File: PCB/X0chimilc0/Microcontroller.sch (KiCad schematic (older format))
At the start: 4 parts, among them T1 SDS-50J, T2 SDS-50J, T3 SDS-50J, U1 STM32H745XIH6

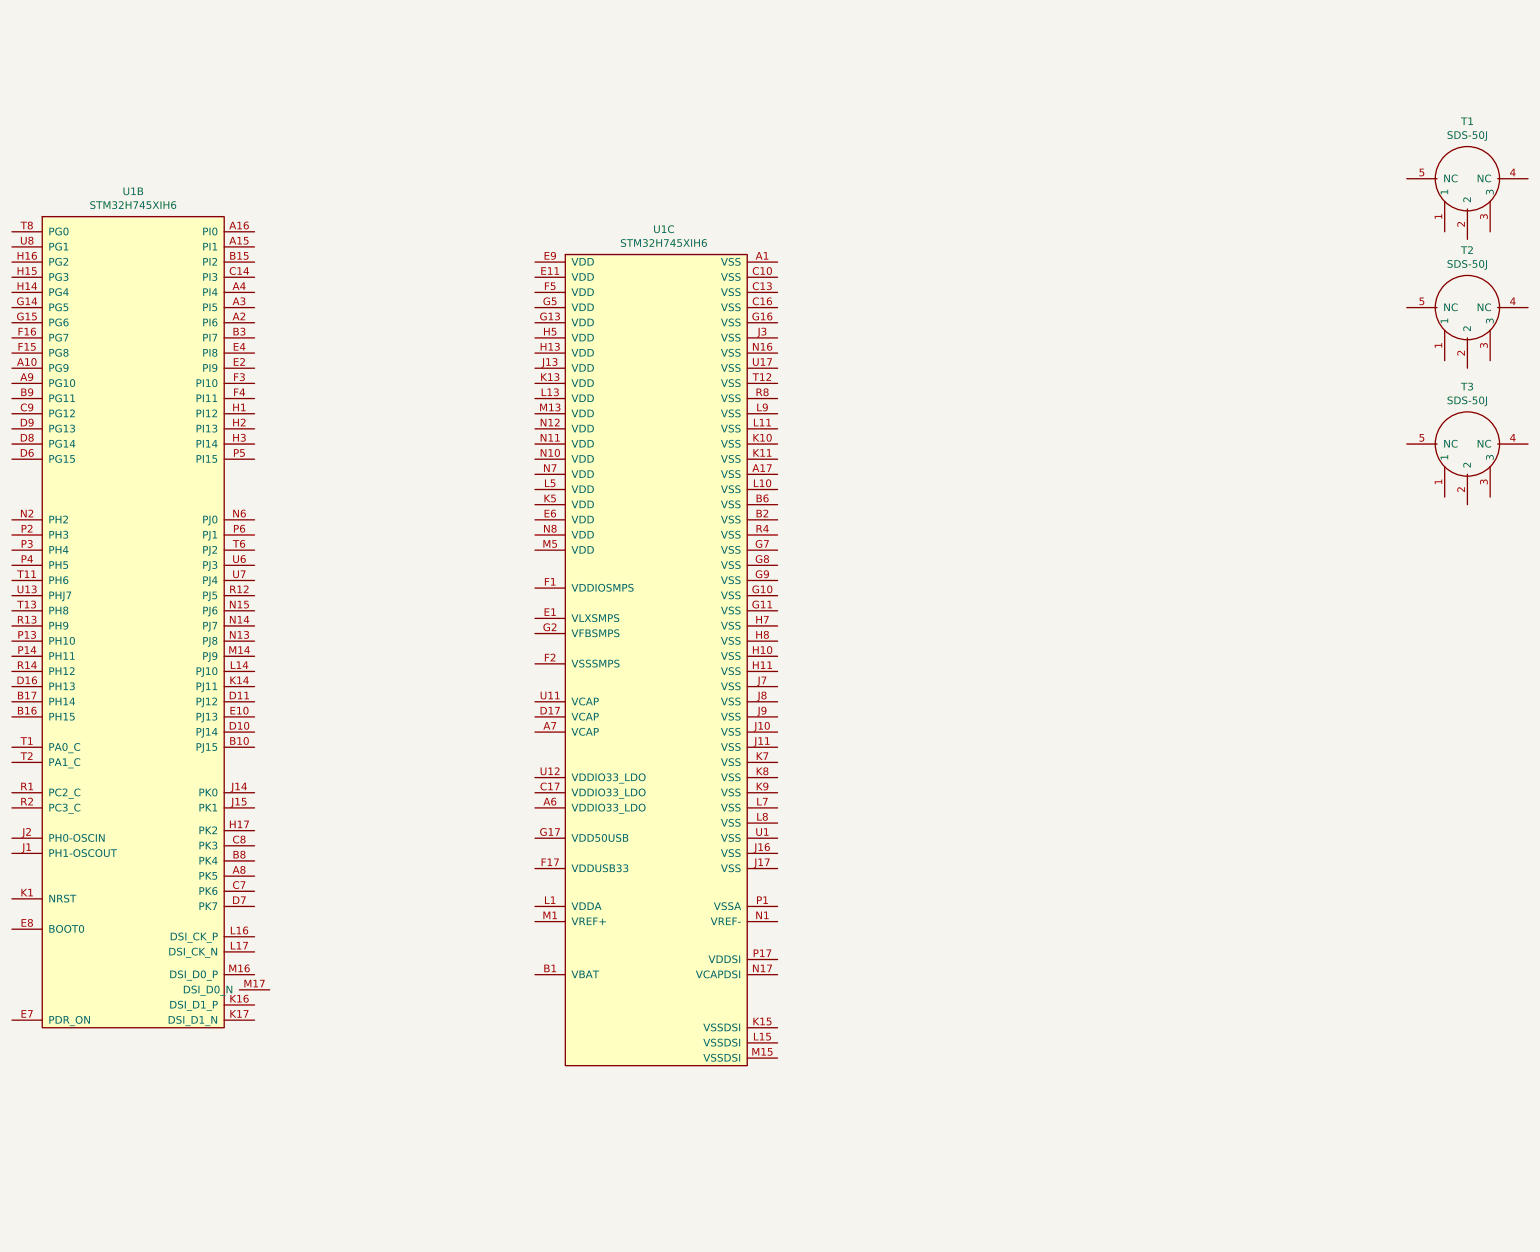
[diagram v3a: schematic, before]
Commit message: MCU Power
MCU power schematic completed, working on other MCU part and Codec.
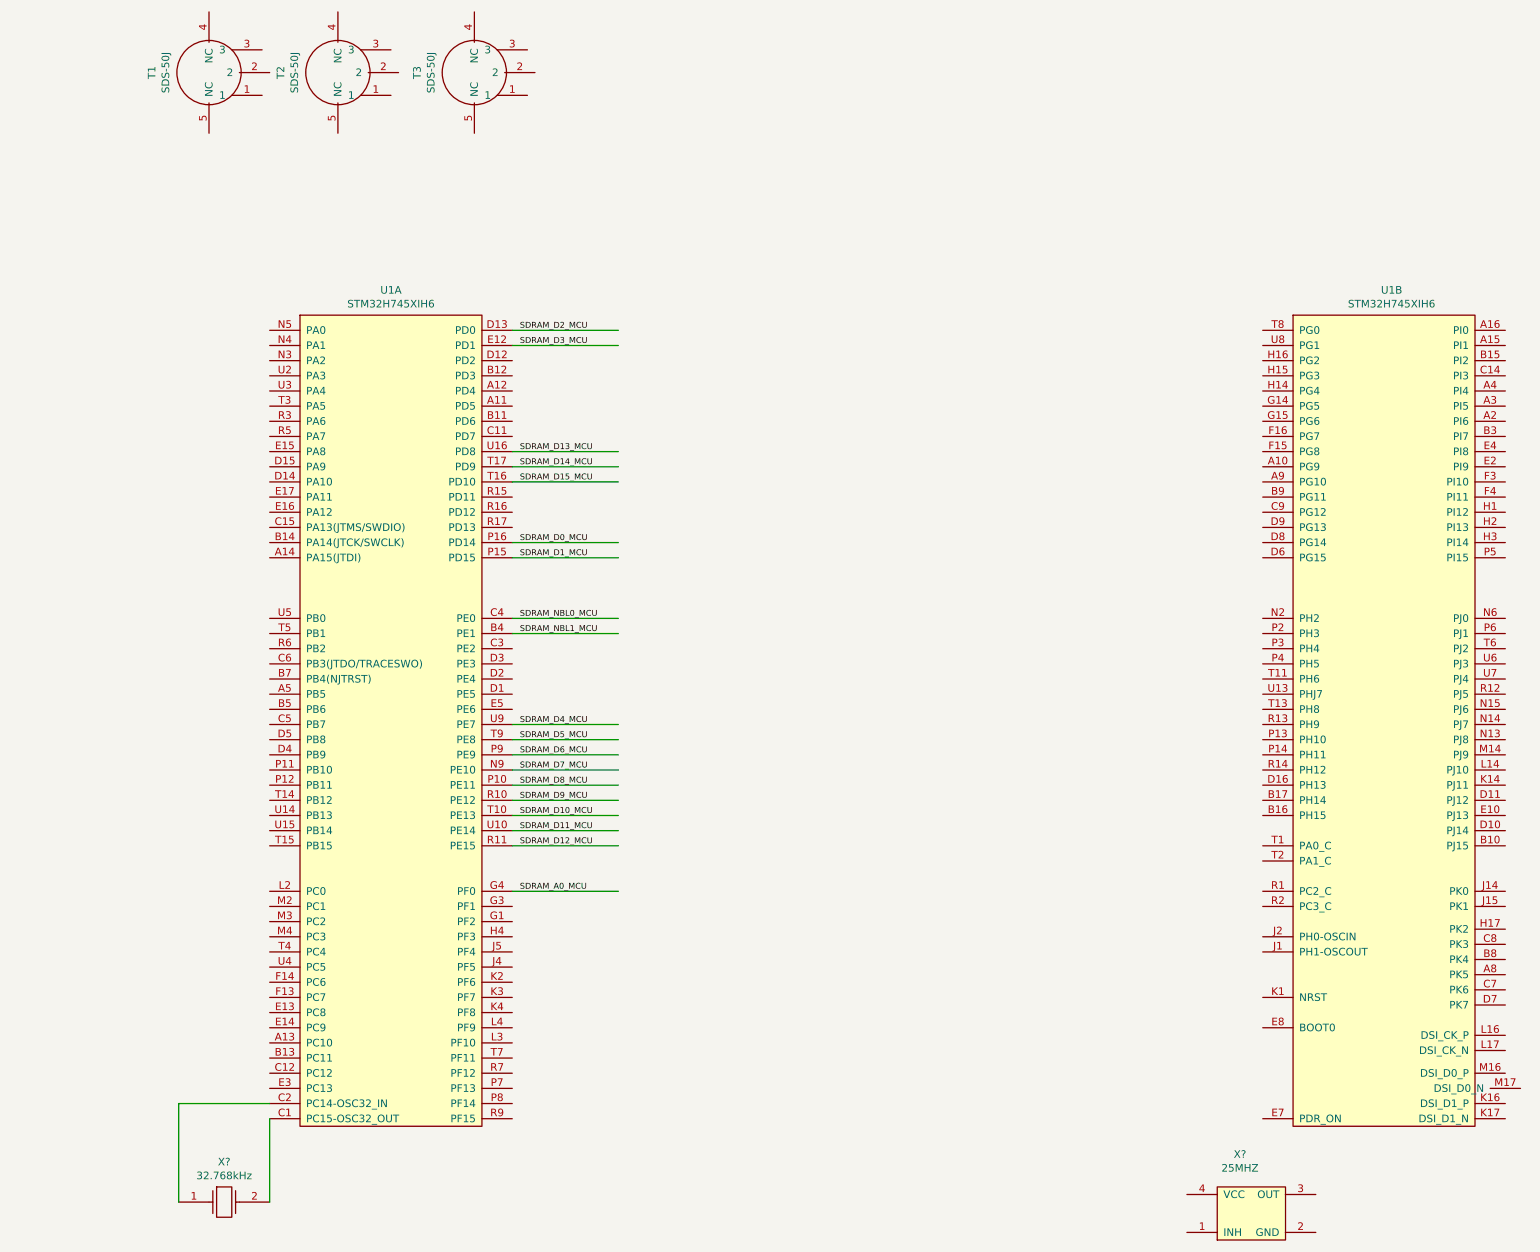
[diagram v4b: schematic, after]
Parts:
- removed unit 3 of U1
- added unit 1 of U1
- added X?: KC2016K25.0000C1GE00, AVR-KiCAD-Lib-Oscillators:KC2016K25.0000C1GE00, symbol AVR-KiCAD-Lib-Oscillators-Clocks:KC2016K25.0000C1GE00
- added X?: NX3215SA-32.768K-STD-MUA-8, AVR-KiCAD-Lib-Oscillators:NX3215SA-32.768K-STD-MUA-8, symbol AVR-KiCAD-Lib-Oscillators-Clocks:NX3215SA-32.768K-STD-MUA-8
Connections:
- net labels added: SDRAM_A0_MCU, SDRAM_D0_MCU, SDRAM_D10_MCU, SDRAM_D11_MCU, SDRAM_D12_MCU, SDRAM_D13_MCU, SDRAM_D14_MCU, SDRAM_D15_MCU, SDRAM_D1_MCU, SDRAM_D2_MCU, SDRAM_D3_MCU, SDRAM_D4_MCU, SDRAM_D5_MCU, SDRAM_D6_MCU, SDRAM_D7_MCU, SDRAM_D8_MCU, SDRAM_D9_MCU, SDRAM_NBL0_MCU, SDRAM_NBL1_MCU
- wire segments 0 -> 22
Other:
- moved on the sheet: T1, T2, T3

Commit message: USB C DDR3L MCU
more with MCU and USB C and DDR3L
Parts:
- added C?: C0402C104K9PACTU, AVR-KiCAD-Lib-Resistors:R0402, symbol AVR-KiCAD-Lib-Capacitors:C0402C104K9PACTU
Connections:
- net labels added: +3V3, AUDIO_I2C_SCL, AUDIO_I2C_SDA, AUDIO_INT, GNDD, JTAG_JTCK_SWCLK, JTAG_JTDI, JTAG_JTDO_TRACESWO, JTAG_JTMS_SWDIO, JTAG_NJRST, SAI2_FSA, SAI2_MCLKA, SAI2_SCKA, SAI2_SDA, SAI2_SDB, USB_C1_D+, USB_C1_D-
- wire segments 22 -> 44
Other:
- moved on the sheet: X?
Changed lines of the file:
@@
 $Descr A3 16535 11693
 encoding utf-8
-Sheet 3 10
+Sheet 2 11
 Title ""
 Date ""
@@
 L AVR-KiCAD-Lib-Oscillators-Clocks:KC2016K25.0000C1GE00 X?
 U 1 1 5E504131
-P 10700 8550
-F 0 "X?" H 10700 8815 50  0000 C CNN
-F 1 "KC2016K25.0000C1GE00" H 10750 8750 50  0001 C CNN
-F 2 "AVR-KiCAD-Lib-Oscillators:KC2016K25.0000C1GE00" H 10500 8550 50  0001 C CNN
-F 3 "https://global.kyocera.com/prdct/electro/product/pdf/clock_k_e.pdf" H 10600 8650 50  0001 C CNN
-F 4 "1.36000" H 10800 8800 50  0001 C CNN "Cost QTY: 1"
-F 5 "0.89238" H 10900 8900 50  0001 C CNN "Cost QTY: 1000"
-F 6 "0.81125" H 11000 9000 50  0001 C CNN "Cost QTY: 2500"
-F 7 "0.77000" H 11100 9100 50  0001 C CNN "Cost QTY: 5000"
-F 8 "0.71500" H 11200 9200 50  0001 C CNN "Cost QTY: 10000"
-F 9 "Kyocera International Inc. Electronic Components" H 11300 9300 50  0001 C CNN "MFR"
-F 10 "KC2016K25.0000C1GE00" H 11400 9400 50  0001 C CNN "MFR#"
-F 11 "Digikey" H 11500 9500 50  0001 C CNN "Vendor"
-F 12 "1253-1567-1-ND" H 11600 9600 50  0001 C CNN "Vendor #"
-F 13 "AVR" H 11700 9700 50  0001 C CNN "Designer"
-F 14 "0.8mm" H 11800 9800 50  0001 C CNN "Height"
-F 15 "12/7/2019" H 12900 10900 50  0001 C CNN "Date Created"
-F 16 "12/7/2019" H 11900 9900 50  0001 C CNN "Date Modified"
-F 17 "Yes" H 12000 10000 50  0001 C CNN "Lead-Free ?"
-F 18 "1" H 12100 10100 50  0001 C CNN "RoHS Levels"
-F 19 "SMT" H 12200 10200 50  0001 C CNN "Mounting"
-F 20 "4" H 12300 10300 50  0001 C CNN "Pin Count #"
-F 21 "Active" H 12400 10400 50  0001 C CNN "Status"
-F 22 "*" H 12500 10500 50  0001 C CNN "Tolerance"
-F 23 "Crystal Oscillator" H 12600 10600 50  0001 C CNN "Type"
-F 24 "1.6-3.6V" H 12700 10700 50  0001 C CNN "Voltage"
-F 25 "*" H 12800 10850 50  0001 C CNN "Package"
-F 26 "25MHz XO (Standard) CMOS Oscillator 1.6V ~ 3.63V Standby (Power Down) 4-SMD, No Lead" H 13100 11150 50  0001 C CNN "Description"
-F 27 "25MHZ" H 10700 8724 50  0000 C CNN "_Value_"
-F 28 "*" H 13100 11150 50  0001 C CNN "Management_ID"
-	1    10700 8550
+P 9750 8700
+F 0 "X?" H 9750 8965 50  0000 C CNN
+F 1 "KC2016K25.0000C1GE00" H 9800 8900 50  0001 C CNN
+F 2 "AVR-KiCAD-Lib-Oscillators:KC2016K25.0000C1GE00" H 9550 8700 50  0001 C CNN
+F 3 "https://global.kyocera.com/prdct/electro/product/pdf/clock_k_e.pdf" H 9650 8800 50  0001 C CNN
+F 4 "1.36000" H 9850 8950 50  0001 C CNN "Cost QTY: 1"
+F 5 "0.89238" H 9950 9050 50  0001 C CNN "Cost QTY: 1000"
+F 6 "0.81125" H 10050 9150 50  0001 C CNN "Cost QTY: 2500"
+F 7 "0.77000" H 10150 9250 50  0001 C CNN "Cost QTY: 5000"
+F 8 "0.71500" H 10250 9350 50  0001 C CNN "Cost QTY: 10000"
+F 9 "Kyocera International Inc. Electronic Components" H 10350 9450 50  0001 C CNN "MFR"
+F 10 "KC2016K25.0000C1GE00" H 10450 9550 50  0001 C CNN "MFR#"
+F 11 "Digikey" H 10550 9650 50  0001 C CNN "Vendor"
+F 12 "1253-1567-1-ND" H 10650 9750 50  0001 C CNN "Vendor #"
+F 13 "AVR" H 10750 9850 50  0001 C CNN "Designer"
+F 14 "0.8mm" H 10850 9950 50  0001 C CNN "Height"
+F 15 "12/7/2019" H 11950 11050 50  0001 C CNN "Date Created"
+F 16 "12/7/2019" H 10950 10050 50  0001 C CNN "Date Modified"
+F 17 "Yes" H 11050 10150 50  0001 C CNN "Lead-Free ?"
+F 18 "1" H 11150 10250 50  0001 C CNN "RoHS Levels"
+F 19 "SMT" H 11250 10350 50  0001 C CNN "Mounting"
+F 20 "4" H 11350 10450 50  0001 C CNN "Pin Count #"
+F 21 "Active" H 11450 10550 50  0001 C CNN "Status"
+F 22 "*" H 11550 10650 50  0001 C CNN "Tolerance"
+F 23 "Crystal Oscillator" H 11650 10750 50  0001 C CNN "Type"
+F 24 "1.6-3.6V" H 11750 10850 50  0001 C CNN "Voltage"
+F 25 "*" H 11850 11000 50  0001 C CNN "Package"
+F 26 "25MHz XO (Standard) CMOS Oscillator 1.6V ~ 3.63V Standby (Power Down) 4-SMD, No Lead" H 12150 11300 50  0001 C CNN "Description"
+F 27 "25MHZ" H 9750 8874 50  0000 C CNN "_Value_"
+F 28 "*" H 12150 11300 50  0001 C CNN "Management_ID"
+	1    9750 8700
 	1    0    0    -1
 $EndComp
@@
 Text Label 5950 6550 0    39   ~ 0
 SDRAM_A0_MCU
+Text GLabel 15300 3350 2    50   Output ~ 0
+SAI2_SCKA
+Text GLabel 15300 3550 2    50   Output ~ 0
+SAI2_FSA
+Text GLabel 15300 3450 2    50   Output ~ 0
+SAI2_SDA
+Text GLabel 9950 3550 0    50   Output ~ 0
+AUDIO_INT
+Text GLabel 15300 3250 2    50   Output ~ 0
+SAI2_MCLKA
+Wire Wire Line
+	12450 3350 15300 3350
+Wire Wire Line
+	12450 3250 15300 3250
+Wire Wire Line
+	12450 3450 15300 3450
+Wire Wire Line
+	12450 3550 15300 3550
+Text GLabel 9950 3850 0    50   Input ~ 0
+SAI2_SDB
+Wire Wire Line
+	10850 3850 9950 3850
+Wire Wire Line
+	9950 3550 10850 3550
+Text GLabel 7250 4150 2    50   BiDi ~ 0
+AUDIO_I2C_SDA
+Text GLabel 7250 4050 2    50   BiDi ~ 0
+AUDIO_I2C_SCL
+Wire Wire Line
+	5900 4150 7250 4150
+Wire Wire Line
+	7250 4050 5900 4050
+Text GLabel 1050 4050 0    50   BiDi ~ 0
+USB_C1_D+
+Text GLabel 1050 3950 0    50   BiDi ~ 0
+USB_C1_D-
+Wire Wire Line
+	1050 3950 4300 3950
+Wire Wire Line
+	4300 4050 1050 4050
+Text GLabel 3700 5150 0    50   BiDi ~ 0
+JTAG_NJRST
+Text GLabel 3700 5050 0    50   BiDi ~ 0
+JTAG_JTDO_TRACESWO
+Text GLabel 3550 4350 0    50   BiDi ~ 0
+JTAG_JTDI
+Text GLabel 3550 4250 0    50   BiDi ~ 0
+JTAG_JTCK_SWCLK
+Text GLabel 3550 4150 0    50   BiDi ~ 0
+JTAG_JTMS_SWDIO
+Wire Wire Line
+	3550 4150 4300 4150
+Wire Wire Line
+	4300 4250 3550 4250
+Wire Wire Line
+	3550 4350 4300 4350
+Wire Wire Line
+	3700 5050 4300 5050
+Wire Wire Line
+	3700 5150 4300 5150
+$Comp
+L AVR-KiCAD-Lib-Capacitors:C0402C104K9PACTU C?
+U 1 1 5ED350F1
+P 8250 8900
+F 0 "C?" V 8229 9028 50  0000 L CNN
+F 1 "C0402C104K9PACTU" H 8300 9100 50  0001 C CNN
+F 2 "AVR-KiCAD-Lib-Resistors:R0402" H 8050 8900 50  0001 C CNN
+F 3 "https://content.kemet.com/datasheets/KEM_C1006_X5R_SMD.pdf" H 8150 9000 50  0001 C CNN
+F 4 "0.10000" H 8350 9150 50  0001 C CNN "Cost QTY: 1"
+F 5 "0.01139" H 8450 9250 50  0001 C CNN "Cost QTY: 1000"
+F 6 "0.01035" H 8550 9350 50  0001 C CNN "Cost QTY: 2500"
+F 7 "0.00952" H 8650 9450 50  0001 C CNN "Cost QTY: 5000"
+F 8 "0.00756" H 8750 9550 50  0001 C CNN "Cost QTY: 10000"
+F 9 "KEMET" H 8850 9650 50  0001 C CNN "MFR"
+F 10 "C0402C104K9PACTU" H 8950 9750 50  0001 C CNN "MFR#"
+F 11 "Digikey" H 9050 9850 50  0001 C CNN "Vendor"
+F 12 "399-3026-6-ND" H 9150 9950 50  0001 C CNN "Vendor #"
+F 13 "AVR" H 9250 10050 50  0001 C CNN "Designer"
+F 14 "0.55mm" H 9350 10150 50  0001 C CNN "Height"
+F 15 "12/7/2019" H 10450 11250 50  0001 C CNN "Date Created"
+F 16 "12/7/2019" H 9450 10250 50  0001 C CNN "Date Modified"
+F 17 "Yes" H 9550 10350 50  0001 C CNN "Lead-Free ?"
+F 18 "1" H 9650 10450 50  0001 C CNN "RoHS Levels"
+F 19 "SMT" H 9750 10550 50  0001 C CNN "Mounting"
+F 20 "2" H 9850 10650 50  0001 C CNN "Pin Count #"
+F 21 "Active" H 9950 10750 50  0001 C CNN "Status"
+F 22 "10%" H 10050 10850 50  0001 C CNN "Tolerance"
+F 23 "Ceramic Cap" H 10150 10950 50  0001 C CNN "Type"
+F 24 "6.3V" H 10250 11050 50  0001 C CNN "Voltage"
+F 25 "0402" H 10350 11200 50  0001 C CNN "Package"
+F 26 "0.1µF ±10% 6.3V Ceramic Capacitor X5R 0402 (1005 Metric)" H 10750 11600 50  0001 C CNN "Description"
+F 27 "0.1uF X5R" V 8320 9028 50  0000 L CNN "_Value_"
+F 28 "*" H 10650 11500 50  0001 C CNN "Management_ID"
+	1    8250 8900
+	0    1    1    0
+$EndComp
+Wire Wire Line
+	9400 8700 8250 8700
+Wire Wire Line
+	7900 8700 7900 8550
+Connection ~ 8250 8700
+Wire Wire Line
+	8250 8700 7900 8700
+$Comp
+L power:GNDD #PWR?
+U 1 1 5ED402AA
+P 10400 8950
+F 0 "#PWR?" H 10400 8700 50  0001 C CNN
+F 1 "GNDD" H 10404 8795 50  0000 C CNN
+F 2 "" H 10400 8950 50  0001 C CNN
+F 3 "" H 10400 8950 50  0001 C CNN
+	1    10400 8950
+	1    0    0    -1
+$EndComp
+$Comp
+L power:+3V3 #PWR?
+U 1 1 5ED41C48
+P 7900 8550
+F 0 "#PWR?" H 7900 8400 50  0001 C CNN
+F 1 "+3V3" H 7915 8723 50  0000 C CNN
+F 2 "" H 7900 8550 50  0001 C CNN
+F 3 "" H 7900 8550 50  0001 C CNN
+	1    7900 8550
+	1    0    0    -1
+$EndComp
+$Comp
+L power:GNDD #PWR?
+U 1 1 5ED44BC6
+P 8250 9150
+F 0 "#PWR?" H 8250 8900 50  0001 C CNN
+F 1 "GNDD" H 8254 8995 50  0000 C CNN
+F 2 "" H 8250 9150 50  0001 C CNN
+F 3 "" H 8250 9150 50  0001 C CNN
+	1    8250 9150
+	1    0    0    -1
+$EndComp
+Wire Wire Line
+	10250 8950 10400 8950
+Wire Wire Line
+	10850 6850 10350 6850
+Wire Wire Line
+	10350 6850 10350 8700
+Wire Wire Line
+	10350 8700 10250 8700
 $EndSCHEMATC
